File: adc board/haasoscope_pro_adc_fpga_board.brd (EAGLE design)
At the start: 220 x 160 mm, 558 parts, among them CN2 12Vin, IC1 ADC12DL2500ACF, IC13 LMH5401IRMST, IC14 LMH6401IRMZR, IC15 SN74AVC4T774PWR, IC17 DAC8562SDGSR, IC18 TLV9102IPWR, IC2 SN74AVC4T774PWR, IC21 LMH5401IRMST, IC22 TPS7A7200RGTR, IC23 TPS7A7200RGTR, IC24 TPS7A7200RGTR, IC25 TPS72325DBVR, IC26 TPS7A7200RGTR, IC27 TPS7A7200RGTR, IC28 TPS7A7200RGTR, IC29 LMH6401IRMZR, IC3 ADC102S021CIMM_NOPB, IC30 SN74AVC4T774PWR, IC33 TLV9102IPWR, IC4 TLV9102IPWR, IC5 EP4CE30F23C6N, IC6 EPCQ16ASI8N, IC8 FT232HQ, IC9 93LC56B, J10 8pin, J11 8pin, J13 8pin, J14 2x5, J15 test1, J2 test1, J30 2p-2.54, J31 2p-2.54, J32 2p-2.54, J33 2p-2.54, J34 2p-2.54, J35 2p-2.54, J36 2p-2.54, J37 2p-2.54, J39 2p-2.54, J40 2p-2.54, J41 2p-2.54, J42 2p-2.54, J43 2p-2.54, J44 2p-2.54, J45 2p-2.54, J46 2p-2.54, J8 8pin, K10 G6K-2F-RF-DC3, K11 G6K-2F-RF-DC3, K12 G6K-2F-RF-DC3, K5 AQY21SOP, K6 G6K-2F-RF-DC3, K7 G6K-2F-RF-DC3, K9 AQY21SOP, Q4 S8050, Q5 S8050, Q7 S8050, Q8 S8050, Q9 S8050, SW3 SKQGADE010, SW4 SKQGADE010, U2 ADF4350BCPZ, U6 AMS1117-1.2, X1 USBC, Y2 OSCILLATORSMD-5X3, Y3 12MHz

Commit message: add 10kHz output for probe comp
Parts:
- added J1: 2p-2.54, Seeed-Connector:H2-2.54
- added R206: 1k, FlashPCB_Resistors:RES-0402
- added R207: NCP18WF104F03RC, Seeed-Resistor:R0603
- R130: value 0 -> 10k
- turned R130 to 180 degrees
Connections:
- new net 10KHZOUT: J1.1, R206.P$1
- net 3V3: now also R130.1
- net BOARDOUT3: now also R206.P$2
- net GND: now also J1.2, R207.1
- net SLOWADCIN2: now also R207.2
- net VD11: no longer R130.1
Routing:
- net BOARDOUT3: track 68.5 -> 259.4 mm, vias 1 -> 3
- net VD11: track 102.9 -> 76.8 mm, vias 10 -> 9
- net SLOWADCIN2: track 1.63 -> 14.6 mm, vias 0 -> 2
- net 10KHZOUT: track 0.00 -> 2.96 mm
- net GND: track 406.8 -> 407.8 mm, vias 462 -> 463
- net 3V3: track 150.1 -> 150.7 mm, vias 24 -> 25
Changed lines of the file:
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@@
 <drawing>
 <settings>
-<setting alwaysvectorfont="no"/>
+<setting alwaysvectorfont="yes"/>
 <setting verticaltext="up"/>
 </settings>
@@
 <element name="R128" library="passives" package="0402_RES" value="0" x="60" y="74.5" smashed="yes" rot="R180"/>
 <element name="R129" library="passives" package="0402_RES" value="0" x="105" y="105" smashed="yes"/>
-<element name="R130" library="passives" package="0402_RES" value="0" x="110.5" y="100" smashed="yes"/>
+<element name="R130" library="passives" package="0402_RES" value="10k" x="110.5" y="100" smashed="yes" rot="R180"/>
 <element name="C50" library="passives" package="0402_CAP" value="0.1uF" x="113.5" y="102" smashed="yes" rot="R270"/>
 <element name="C84" library="MF_Passives" package="C0402" value="0.1uF" x="67.5" y="41.5" smashed="yes" rot="R180">
@@
 <attribute name="VALUE" x="108" y="100" size="0.8128" layer="27" align="center"/>
 </element>
+<element name="R206" library="FlashPCB_Resistors" package="RES-0402" value="1k" x="4.6" y="111.22" smashed="yes">
+<attribute name="VALUE" x="3.33" y="111.72" size="0.8128" layer="27" font="vector"/>
+</element>
+<element name="J1" library="Seeed-Connector" library_urn="urn:adsk.eagle:library:478" package="H2-2.54" package3d_urn="urn:adsk.eagle:package:33132/1" value="2p-2.54" x="1.17" y="110.02" smashed="yes">
+<attribute name="MPN" value="P125-1102A0BS116A1" x="1.17" y="110.02" size="1.778" layer="27" display="off"/>
+</element>
+<element name="R207" library="Seeed-Resistor" library_urn="urn:adsk.eagle:library:474" package="R0603" package3d_urn="urn:adsk.eagle:package:32791/1" value="NCP18WF104F03RC" x="99" y="98.5" smashed="yes" rot="R90">
+<attribute name="LCSC" value="C13564" x="99" y="98.5" size="1.778" layer="27" rot="R90" display="off"/>
+<attribute name="MPN" value="NCP18XH103F03RB" x="99" y="98.5" size="1.778" layer="27" rot="R90" display="off"/>
+<attribute name="VALUE" x="104.605" y="97.435" size="0.8128" layer="21" ratio="10" rot="R180"/>
+</element>
 </elements>
 <signals>
@@
 <wire x1="70.5" y1="41.9" x2="70.742" y2="41.658" width="0.1524" layer="1"/>
 <wire x1="72.5" y1="42.5" x2="72.5" y2="41.9" width="0.1524" layer="1"/>
-<wire x1="72.5" y1="41.9" x2="72.258" y2="41.658" width="0.1524" layer="1"/>
-<wire x1="72.258" y1="41.658" x2="72.25" y2="41.65" width="0.1524" layer="1"/>
+<wire x1="72.5" y1="41.9" x2="72.25" y2="41.65" width="0.1524" layer="1"/>
 <via x="68.5" y="33.5" extent="1-16" drill="0.35"/>
 <wire x1="69.95" y1="33.5" x2="68.5" y2="33.5" width="0.1524" layer="1"/>
@@
 <via x="24.5" y="73.5" extent="1-16" drill="0.35"/>
 <via x="41" y="61" extent="1-16" drill="0.35"/>
+<contactref element="J1" pad="2"/>
+<contactref element="R207" pad="1"/>
+<via x="97.25" y="98.55" extent="1-16" drill="0.5"/>
+<wire x1="97.25" y1="98.55" x2="98.188" y2="98.55" width="0.1524" layer="1"/>
+<wire x1="98.188" y1="98.55" x2="98.238" y2="98.5" width="0.1524" layer="1"/>
 </signal>
 <signal name="3V3" class="1">
@@
 <wire x1="141.3012" y1="80.8012" x2="141.5" y2="81" width="0.1524" layer="14"/>
 <wire x1="141.3012" y1="79.69845625" x2="141.3012" y2="80.8012" width="0.1524" layer="14"/>
+<contactref element="R130" pad="1"/>
+<via x="111.55" y="99.95" extent="1-16" drill="0.35"/>
+<wire x1="110.93306875" y1="100" x2="111.5" y2="100" width="0.1524" layer="1"/>
+<wire x1="111.5" y1="100" x2="111.55" y2="99.95" width="0.1524" layer="1"/>
 </signal>
 <signal name="DC2_P" class="2">
@@
 <wire x1="74.55" y1="77.05" x2="74.55" y2="76.05" width="0.1524" layer="16"/>
 <wire x1="74.55" y1="76.05" x2="74.5" y2="76" width="0.1524" layer="16"/>
-<contactref element="R130" pad="1"/>
 <wire x1="79.15" y1="97.6" x2="79.6" y2="97.6" width="1.27" layer="1"/>
 <wire x1="79.6" y1="97.6" x2="80" y2="98" width="1.27" layer="1"/>
@@
 <wire x1="125.95" y1="132.5" x2="127.5" y2="132.5" width="1.27" layer="1"/>
 <wire x1="128.5" y1="132.5" x2="131.775" y2="132.5" width="1.27" layer="1"/>
-<wire x1="110.06693125" y1="100" x2="109" y2="100" width="0.254" layer="1"/>
-<via x="109" y="100" extent="1-16" drill="0.2"/>
-<wire x1="109" y1="100" x2="88.5" y2="100" width="0.254" layer="5"/>
-<wire x1="88.5" y1="100" x2="85.25" y2="103.25" width="0.254" layer="5"/>
 </signal>
 <signal name="VLVDS" class="1">
@@
 <wire x1="102.75" y1="20.5" x2="104.125" y2="21.875" width="0.0889" layer="1"/>
 <wire x1="102.75" y1="20.5" x2="102.72" y2="20.5" width="0.0889" layer="1"/>
+<contactref element="R206" pad="P$2"/>
+<wire x1="5.1" y1="111.22" x2="38.28" y2="111.22" width="0.1524" layer="1"/>
+<wire x1="38.28" y1="111.22" x2="38.5" y2="111" width="0.1524" layer="1"/>
+<via x="38.5" y="111" extent="1-16" drill="0.35"/>
+<wire x1="38.5" y1="111" x2="97" y2="111" width="0.1524" layer="3"/>
+<wire x1="97" y1="111" x2="106.5" y2="120.5" width="0.1524" layer="3"/>
+<wire x1="106.5" y1="120.5" x2="115" y2="120.5" width="0.1524" layer="3"/>
+<wire x1="125" y1="110.5" x2="136.5" y2="110.5" width="0.1524" layer="3"/>
+<wire x1="136.5" y1="110.5" x2="136.5" y2="92.28234375" width="0.1524" layer="3"/>
+<wire x1="136.5" y1="92.28234375" x2="136.4468" y2="92.22914375" width="0.1524" layer="3"/>
+<wire x1="136.4468" y1="92.22914375" x2="136.4468" y2="91.77085625" width="0.1524" layer="3"/>
+<wire x1="136.4468" y1="91.77085625" x2="136.5" y2="91.71765625" width="0.1524" layer="3"/>
+<wire x1="136.5" y1="91.71765625" x2="136.5" y2="76.5" width="0.1524" layer="3"/>
+<wire x1="136.5" y1="76.5" x2="131.5" y2="71.5" width="0.1524" layer="3"/>
+<wire x1="131.5" y1="71.5" x2="129" y2="71.5" width="0.1524" layer="3"/>
+<via x="129" y="71.5" extent="1-16" drill="0.35"/>
+<wire x1="129" y1="71.5" x2="122" y2="71.5" width="0.1524" layer="16"/>
+<wire x1="122" y1="71.5" x2="121.5" y2="71" width="0.1524" layer="16"/>
+<wire x1="115" y1="120.5" x2="125" y2="110.5" width="0.1524" layer="3"/>
 </signal>
 <signal name="BOARDOUT4">
@@
 <contactref element="R130" pad="2"/>
 <contactref element="IC4" pad="5"/>
-<wire x1="111" y1="101.5" x2="111" y2="100" width="0.0889" layer="1"/>
-<wire x1="111" y1="100" x2="110.93306875" y2="100" width="0.0889" layer="1"/>
-<wire x1="111" y1="101.5" x2="110.938" y2="101.525" width="0.0889" layer="1"/>
+<wire x1="110.938" y1="101.525" x2="110.38" y2="100.967" width="0.0889" layer="1"/>
+<wire x1="110.38" y1="100.967" x2="110.38" y2="100.31306875" width="0.0889" layer="1"/>
+<wire x1="110.38" y1="100.31306875" x2="110.06693125" y2="100" width="0.0889" layer="1"/>
+<contactref element="R207" pad="2"/>
+<wire x1="99.762" y1="98.5" x2="102.5" y2="98.5" width="0.1524" layer="1"/>
+<via x="102.5" y="98.5" extent="1-16" drill="0.35"/>
+<wire x1="102.5" y1="98.5" x2="104" y2="100" width="0.1524" layer="14"/>
+<wire x1="104" y1="100" x2="108" y2="100" width="0.1524" layer="14"/>
+<wire x1="108" y1="100" x2="109.5" y2="98.5" width="0.1524" layer="14"/>
+<via x="109.5" y="98.5" extent="1-16" drill="0.35"/>
+<wire x1="109.5" y1="98.5" x2="109.5" y2="99.43306875" width="0.1524" layer="1"/>
+<wire x1="109.5" y1="99.43306875" x2="110.06693125" y2="100" width="0.1524" layer="1"/>
 </signal>
 <signal name="AOUT_P" class="2">
@@
 <wire x1="144.1315" y1="73.5115" x2="145.9145" y2="73.5115" width="0.254" layer="1"/>
 </signal>
+<signal name="10KHZOUT">
+<contactref element="R206" pad="P$1"/>
+<contactref element="J1" pad="1"/>
+<wire x1="1.17" y1="111.29" x2="4.03" y2="111.29" width="0.1524" layer="1"/>
+<wire x1="4.03" y1="111.29" x2="4.1" y2="111.22" width="0.1524" layer="1"/>
+</signal>
 </signals>

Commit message: add fan connector and control
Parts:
- added JST_FAN: Fan, SparkFun-Connectors:1X02
- added Q1: S8050, Seeed-Transistor:SOT-23
- added R208: 1k, MF_Passives:R0402
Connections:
- removed net DEBUGOUT11: IC5.B16, J11.8, R30.P$1
- new net FAN-: JST_FAN.2, Q1.3
- new net FAN_CONTROL: IC5.B16, J11.8, R208.P$2, R30.P$1
- new net N$10: Q1.1, R208.P$1
- net 5V: now also JST_FAN.1
- net GND: now also Q1.2
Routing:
- net FAN_CONTROL: track 0.00 -> 181.9 mm, vias 0 -> 4
- net DEBUGOUT11: track 103.6 -> 0.00 mm, vias 2 -> 0
- net FAN-: track 0.00 -> 7.01 mm
- net GND: track 407.8 -> 401.8 mm
- net N$10: track 0.00 -> 5.05 mm
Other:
- board text added: "+"
- board text added: "-"
- board text added: "Fan"
- board text added: "Haasoscope Pro, v1.01 by DrAndyHaas October 2024"
- board text removed: "D11"
- board text removed: "Haasoscope Pro, v1.00 by DrAndyHaas October 2024"

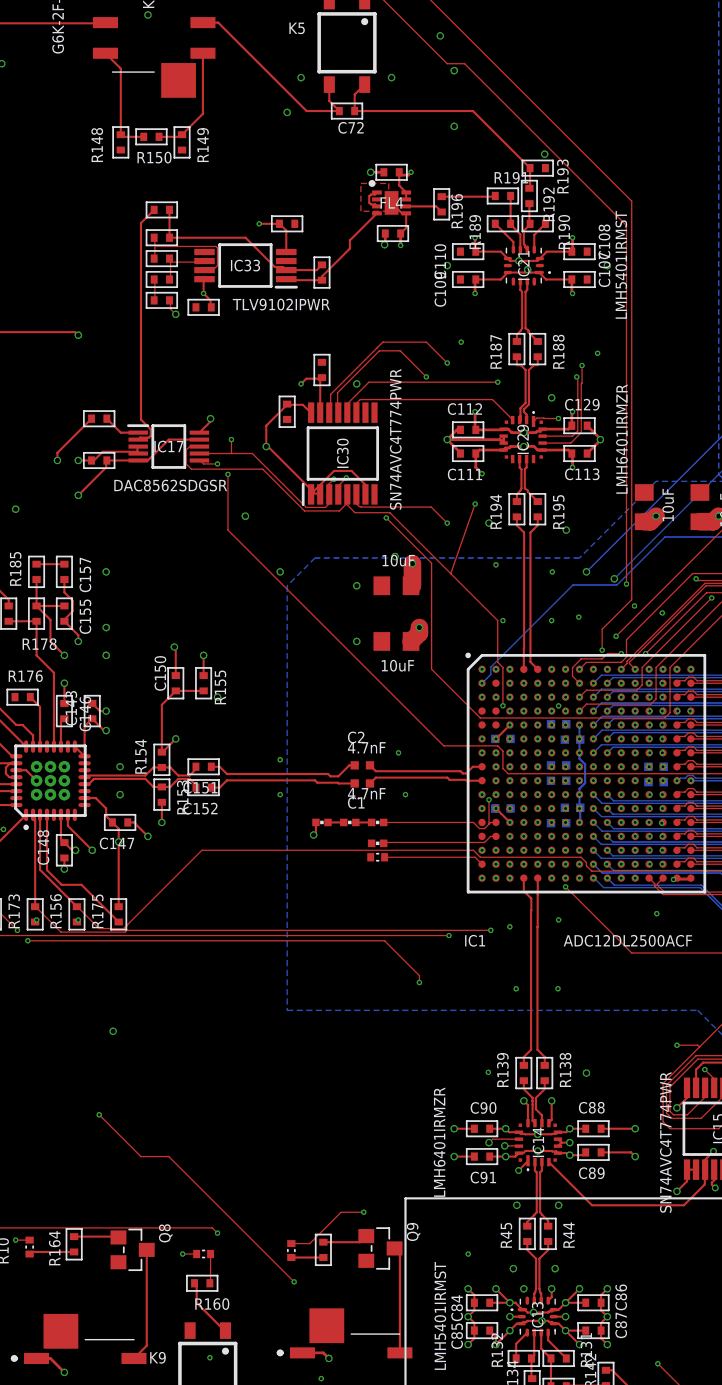
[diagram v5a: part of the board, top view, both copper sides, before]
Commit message: add adiff netclass, 4 mil wide with 5 mil spacing
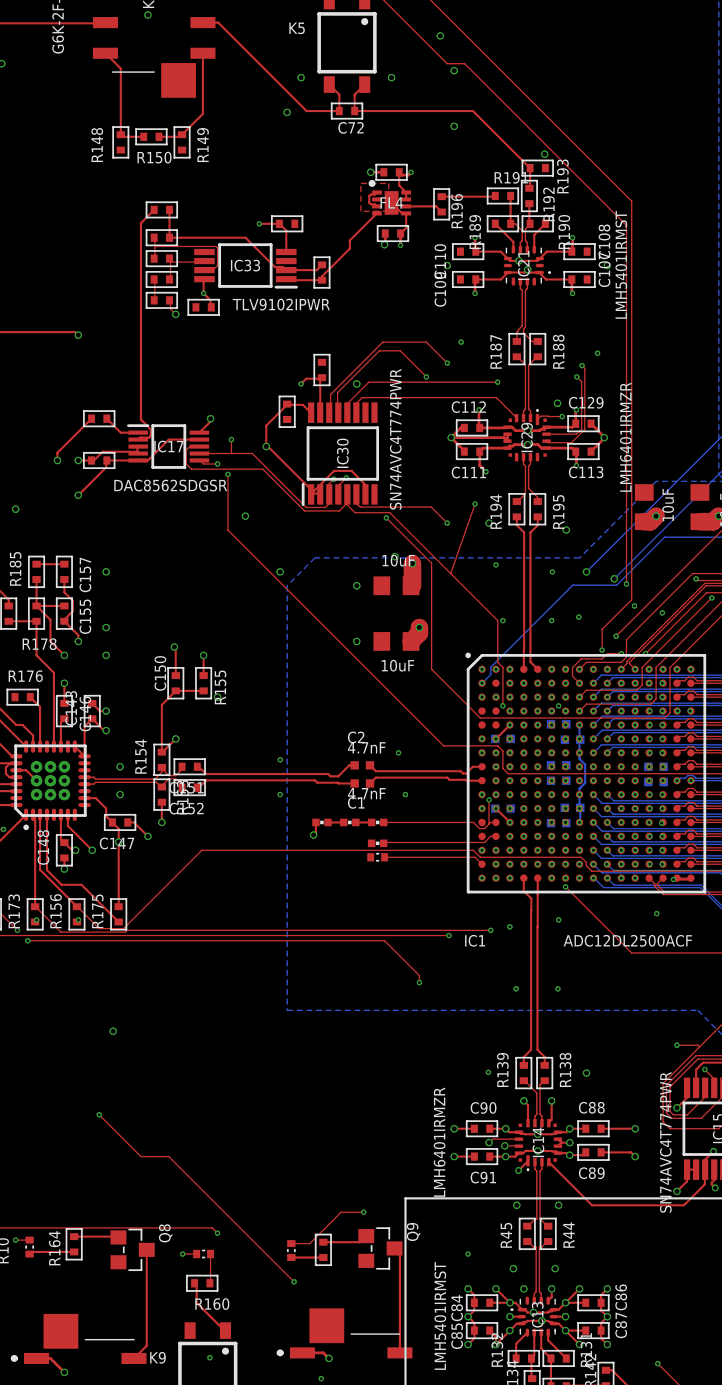
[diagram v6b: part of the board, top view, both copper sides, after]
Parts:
- moved C151 1.00 mm to (46.5, 80.0)
- moved C152 1.00 mm to (46.5, 78.5)
- moved C111 0.31 mm to (66.8, 102.6)
- moved C112 0.31 mm to (66.8, 104.3)
- moved C113 0.31 mm to (74.8, 102.6)
- moved C129 0.31 mm to (74.8, 104.6)
- moved IC29 0.31 mm to (70.8, 103.6)
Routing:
- net RFOUTA_P: track 9.02 -> 7.86 mm
- net CLK_P: track 10.9 -> 11.9 mm
- net CLK_N: track 10.6 -> 11.6 mm
- net RFOUTA_N: track 8.90 -> 8.26 mm
- net AOUTSMA2_N: track 5.35 -> 4.75 mm

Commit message: 12 bit ADC for temp mon (cheaper than 10 bit somehow), change gain from 2 to 1.1 for NTC input
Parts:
- IC3: value ADC102S021CIMM_NOPB -> ADC122S021CIMM_NOPB; device ADC102S021CIMM_NOPB:SOP65P490X110-8N -> ADC122S021CIMM_NOPB:SOP65P490X110-8N
- R125: value 1k -> 10k
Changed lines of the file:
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@@
 <drawing>
 <settings>
-<setting alwaysvectorfont="yes"/>
+<setting alwaysvectorfont="no"/>
 <setting verticaltext="up"/>
 </settings>
@@
 <element name="C41" library="Nordic_nRF" library_urn="urn:adsk.eagle:library:169009" package="RESC0805_N" package3d_urn="urn:adsk.eagle:package:2593736/1" value="10uF" x="117.5" y="108.5" smashed="yes" rot="R270"/>
 <element name="C42" library="Nordic_nRF" library_urn="urn:adsk.eagle:library:169009" package="RESC0805_N" package3d_urn="urn:adsk.eagle:package:2593736/1" value="10uF" x="138.5" y="92" smashed="yes" rot="R270"/>
-<element name="IC3" library="ADC102S021CIMM_NOPB" package="SOP65P490X110-8N" value="ADC102S021CIMM_NOPB" x="117.5" y="102" smashed="yes">
-<attribute name="DESCRIPTION" value="2 Channel, 50 ksps to 200 ksps, 10-Bit A/D Converter" x="117.5" y="102" size="1.778" layer="27" display="off"/>
+<element name="IC3" library="ADC122S021CIMM_NOPB" package="SOP65P490X110-8N" value="ADC122S021CIMM_NOPB" x="117.5" y="102" smashed="yes">
+<attribute name="DESCRIPTION" value="2 Channel, 50 ksps to 200 ksps, 12-Bit A/D Converter" x="117.5" y="102" size="1.778" layer="27" display="off"/>
 <attribute name="HEIGHT" value="1.1mm" x="117.5" y="102" size="1.778" layer="27" display="off"/>
 <attribute name="JLC_ROTATION" value="270" x="0" y="0" size="1.778" layer="27" rot="R270" display="off"/>
 <attribute name="MANUFACTURER_NAME" value="Texas Instruments" x="117.5" y="102" size="1.778" layer="27" display="off"/>
-<attribute name="MANUFACTURER_PART_NUMBER" value="ADC102S021CIMM/NOPB" x="117.5" y="102" size="1.778" layer="27" display="off"/>
-<attribute name="MOUSER_PART_NUMBER" value="926-AD102S021CIMMNPB" x="117.5" y="102" size="1.778" layer="27" display="off"/>
-<attribute name="MOUSER_PRICE-STOCK" value="https://www.mouser.co.uk/ProductDetail/Texas-Instruments/ADC102S021CIMM-NOPB?qs=7X5t%252BdzoRHDLCWKeMhJPog%3D%3D" x="117.5" y="102" size="1.778" layer="27" display="off"/>
+<attribute name="MANUFACTURER_PART_NUMBER" value="ADC122S021CIMM/NOPB" x="117.5" y="102" size="1.778" layer="27" display="off"/>
 </element>
 <element name="C44" library="passives" package="0402_CAP" value="0.1uF" x="110.5" y="105" smashed="yes"/>
 <element name="R126" library="passives" package="0402_RES" value="1k" x="112.5" y="102" smashed="yes" rot="R90"/>
 <element name="R124" library="passives" package="0402_RES" value="1k" x="103" y="101.5" smashed="yes" rot="R90"/>
-<element name="R125" library="passives" package="0402_RES" value="1k" x="112.5" y="100" smashed="yes" rot="R90"/>
+<element name="R125" library="passives" package="0402_RES" value="10k" x="112.5" y="100" smashed="yes" rot="R90"/>
 <element name="R128" library="passives" package="0402_RES" value="0" x="60" y="74.5" smashed="yes" rot="R180"/>
 <element name="R129" library="passives" package="0402_RES" value="0" x="105" y="105" smashed="yes"/>
